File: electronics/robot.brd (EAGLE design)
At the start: 170.3 x 155.9 mm, 73 parts, among them IC1 FT232L, U1 MT3608, U2 ESP32-WROOM-32E_(16MB), U3 IRLMS2002TRPBF, U4 IRLMS2002TRPBF, X1 USB-B

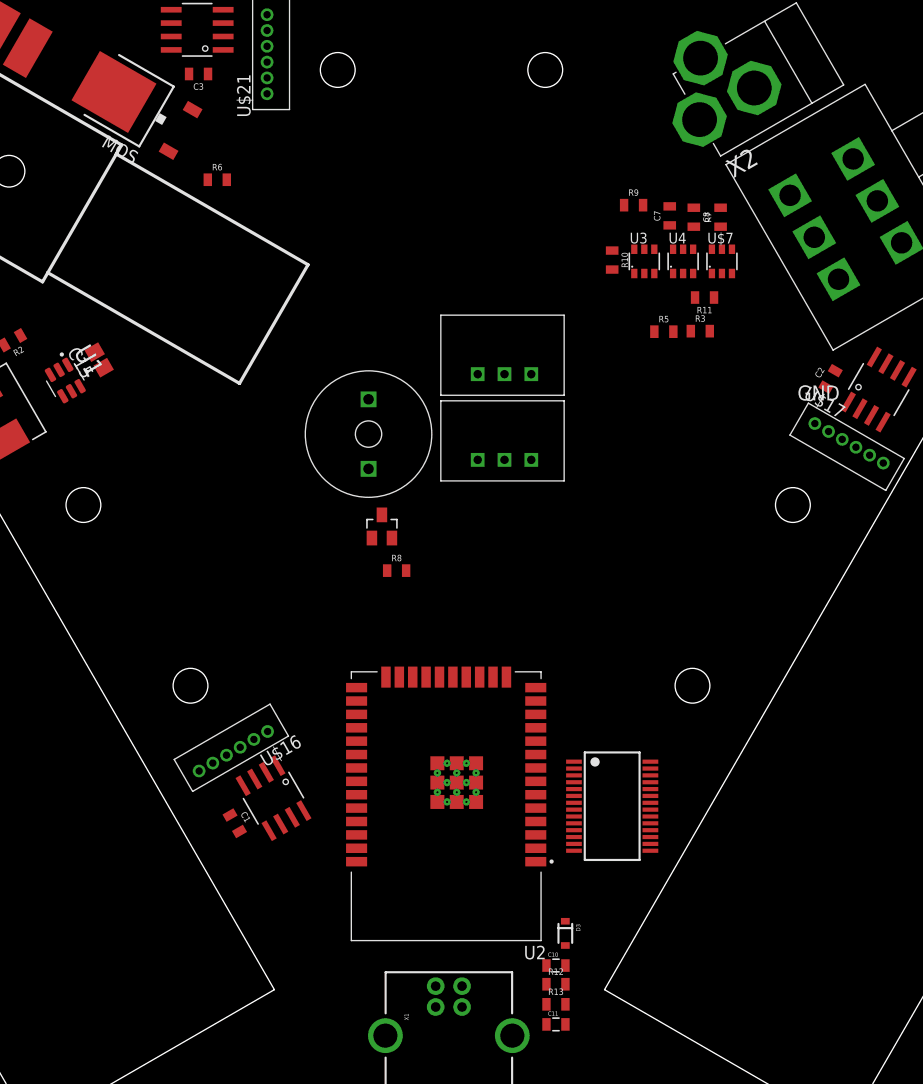
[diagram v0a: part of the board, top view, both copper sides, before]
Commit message: Removing former directories (electronics merged)
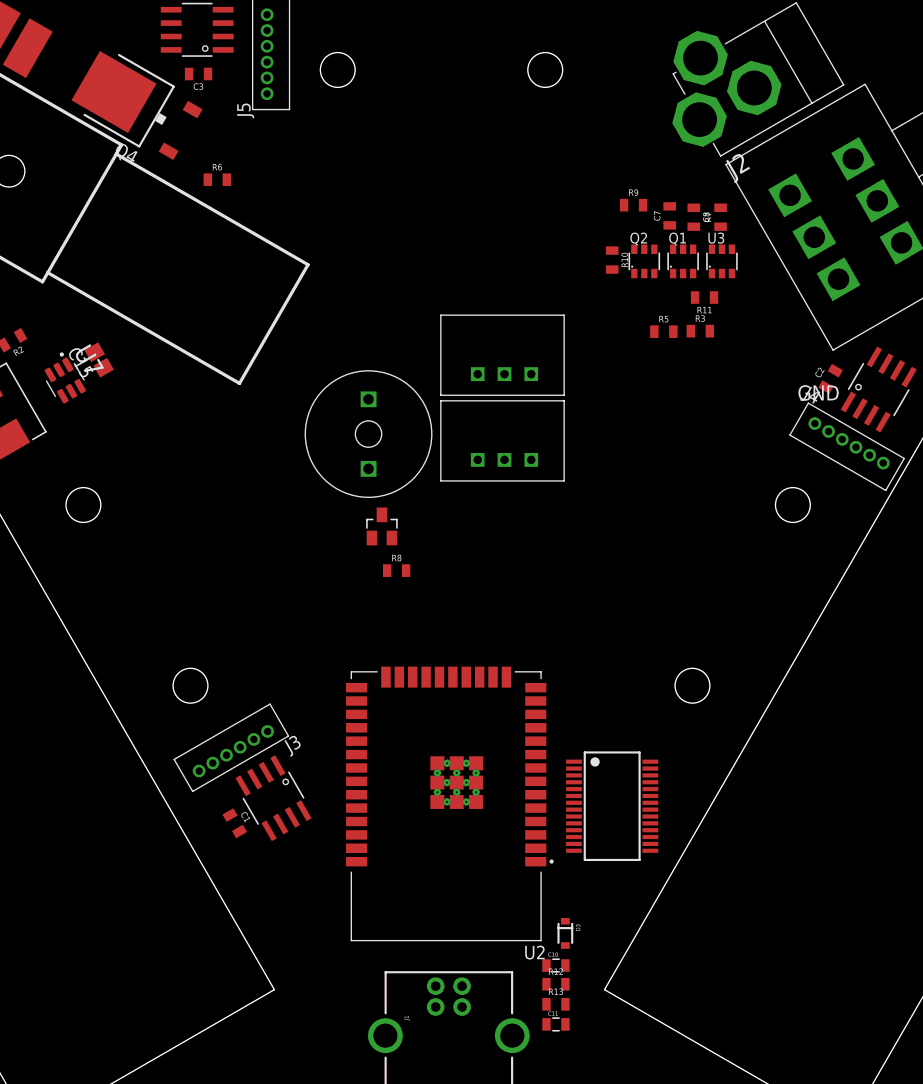
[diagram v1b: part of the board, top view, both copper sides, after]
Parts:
- removed HB1: L9110, rhoban:SO8
- removed IC1: FT232L, rhoban:SSOP28
- removed REG: REG_5V, rhoban:TRACOPOWER
- removed U$7: S8252, rhoban:SOT23-6
- added Q1, Q2: IRLMS2002TRPBF, rhoban:SOT23-6
- added REG2: REG_5V, rhoban:TRACOPOWER
- added U7: MT3608, MT3608:SOT95P280X145-6N
- U1: value MT3608 -> FT232L; device MT3608:SOT95P280X145-6N -> rhoban:SSOP28
- U3: value IRLMS2002TRPBF -> S8252
- U4: value IRLMS2002TRPBF -> L9110; device rhoban:SOT23-6 -> rhoban:SO8
- moved U1 65.7 mm to (16.5, -36.8), turned to 270 degrees
- moved U4 64.1 mm to (-15.6, -36.1), turned to 300 degrees
- moved REG1 8.13 mm to (0.25, 2.16)
- moved U3 7.37 mm to (26.9, 14.9)
- renumbered HB2 to U5, HB3 to U6, KICK_PADS to J6, MOS to Q4, U$12 to Q3, U$13 to B1, U$14 to S1, U$16 to J3, U$17 to J4, U$21 to J5, X1 to J1, X2 to J2
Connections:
- removed net VIN_RAW: C1.1, C2.1, C3.1, HB1.2, HB1.3, U5.2, U5.3, U6.2, U6.3
- net 3.3V: now also REG2.P$3, U1.20, U1.4; no longer IC1.20, IC1.4, REG1.P$3
- net GND: now also Q2.4, REG2.P$2, U1.18, U1.21, U1.25, U1.7, U4.5, U4.8, U7.2; no longer HB1.5, HB1.8, IC1.18, IC1.21, IC1.25, IC1.7, REG.P$2, U1.2, U3.4
- net GND_RAW: now also Q1.4, U3.6; no longer U$7.6, U4.4
- net M1A: now also U4.6; no longer HB1.6
- net M1B: now also U4.7; no longer HB1.7
- net M1P1: now also U4.1; no longer HB1.1
- net M1P2: now also U4.4; no longer HB1.4
- net N$1: now also U7.1; no longer U1.1
- net N$10: now also Q1.1, Q1.2, Q1.5, Q1.6, Q2.1, Q2.2, Q2.5, Q2.6; no longer U3.1, U3.2, U3.5, U3.6, U4.1, U4.2, U4.5, U4.6
- net N$11: now also Q2.3, U3.2; no longer U$7.2, U3.3
- net N$12: now also Q1.3, U3.1; no longer U$7.1, U4.3
- net N$13: now also U3.3; no longer U$7.3
- net N$14: now also U1.1; no longer IC1.1
- net N$15: now also U1.5; no longer IC1.5
- net N$4: now also U7.3; no longer U1.3
- net N$8: now also U3.5; no longer U$7.5
- net N$9: now also U3.4; no longer U$7.4
- net USBDM: now also U1.16; no longer IC1.16
- net USBDP: now also U1.15; no longer IC1.15
- net VCC: now also REG1.P$3; no longer REG.P$3
- net VIN: now also C1.1, C2.1, C3.1, REG2.P$1, U4.2, U4.3, U5.2, U5.3, U6.2, U6.3, U7.4, U7.5; no longer REG.P$1, U1.4, U1.5

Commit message: Autorouting to test
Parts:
- removed D3: (no value), SparkFun-DiscreteSemi:SOD-323
- removed R1: 270, SparkFun-Resistors:0805
- added C9: 0.1µF, SparkFun-Capacitors:0805
- added R14: 270, rcl:R2010
- R6: value 0.3OHM-0805-1/8W-1% -> 3K
- moved C16 5.98 mm to (-39.9, 10.7)
- moved R5 3.51 mm to (17.9, 8.38)
- moved R3 3.28 mm to (21.6, 8.38)
- moved C6 2.74 mm to (-0.76, 71.0)
- moved LED5 2.74 mm to (-0.64, 75.1)
- moved LED6 2.74 mm to (-0.64, 75.1)
- moved C3 2.43 mm to (-20.3, 32.9)
- moved LED1 2.36 mm to (66.7, -36.3)
- moved LED2 2.36 mm to (66.7, -36.3)
- moved C4 2.36 mm to (63.1, -34.1)
- moved R6 2.08 mm to (-22.6, 23.9), turned to 180 degrees
- moved R2 1.78 mm to (-38.6, 7.51)
- moved LED3 1.65 mm to (-66.3, -35.6)
- moved LED4 1.65 mm to (-66.3, -35.6)
- moved C5 1.65 mm to (-62.3, -33.9)
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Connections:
- removed net VUSB: D3.2, J1.VBUS
- new net N$6: U1.1, U2.34
- net GND: now also C9.2, R6.1; no longer R6.2
- net KICK: now also R6.2; no longer R6.1
- net N$14: now also U1.5; no longer U1.1
- net N$15: now also C9.1, U1.17; no longer U1.5, U2.34
- net N$2: now also R14.2; no longer R1.2
- net VCC: now also J1.VBUS, REG2.P$1; no longer D3.1
- net VIN: no longer REG2.P$1
- net VSTORE: now also R14.1; no longer R1.1
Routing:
- net GND: track 0.00 -> 608.9 mm, vias 0 -> 9
- net VCC: track 0.00 -> 393.5 mm, vias 0 -> 4
- net VIN: track 0.00 -> 250.4 mm, vias 0 -> 2
- net N$30: track 0.00 -> 173.1 mm, vias 0 -> 1
- net N$28: track 0.00 -> 170.8 mm, vias 0 -> 1
- net 3.3: track 0.00 -> 133.7 mm
- net LEDS: track 0.00 -> 102.2 mm, vias 0 -> 2
- net M3A: track 0.00 -> 94.2 mm, vias 0 -> 2
- net M3B: track 0.00 -> 92.4 mm, vias 0 -> 2
- net M3C2: track 0.00 -> 86.2 mm, vias 0 -> 1
- net M3C1: track 0.00 -> 78.1 mm, vias 0 -> 2
- net M2B: track 0.00 -> 77.0 mm, vias 0 -> 4
- net KICK: track 0.00 -> 75.0 mm, vias 0 -> 2
- net M2C2: track 0.00 -> 74.4 mm, vias 0 -> 3
- net M2A: track 0.00 -> 71.4 mm, vias 0 -> 4
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- added copper zone on layer 1, net GND
- added copper zone on layer 16, net GND

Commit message: BMS resistors
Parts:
- R10, R9: value 10K -> 470
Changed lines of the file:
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@@
 <attribute name="FARNELL" value="2447662" x="26.797" y="19.05" size="1.778" layer="27" rot="R90" display="off"/>
 </element>
-<element name="R9" library="SparkFun-Resistors" package="0805" value="10K" x="18.542" y="20.193">
+<element name="R9" library="SparkFun-Resistors" package="0805" value="470" x="18.542" y="20.193">
 <attribute name="PROD_ID" value="RES-11622" x="18.542" y="20.193" size="1.778" layer="27" display="off"/>
 <attribute name="VALUE" value="0.3" x="18.542" y="20.193" size="1.778" layer="27" display="off"/>
 <attribute name="FARNELL" value="2074334RL" x="18.542" y="20.193" size="1.778" layer="27" display="off"/>
 </element>
-<element name="R10" library="SparkFun-Resistors" package="0805" value="10K" x="16.51" y="14.986" rot="R270">
+<element name="R10" library="SparkFun-Resistors" package="0805" value="470" x="16.51" y="14.986" rot="R270">
 <attribute name="PROD_ID" value="RES-11622" x="16.51" y="14.986" size="1.778" layer="27" rot="R270" display="off"/>
 <attribute name="VALUE" value="0.3" x="16.51" y="14.986" size="1.778" layer="27" rot="R270" display="off"/>

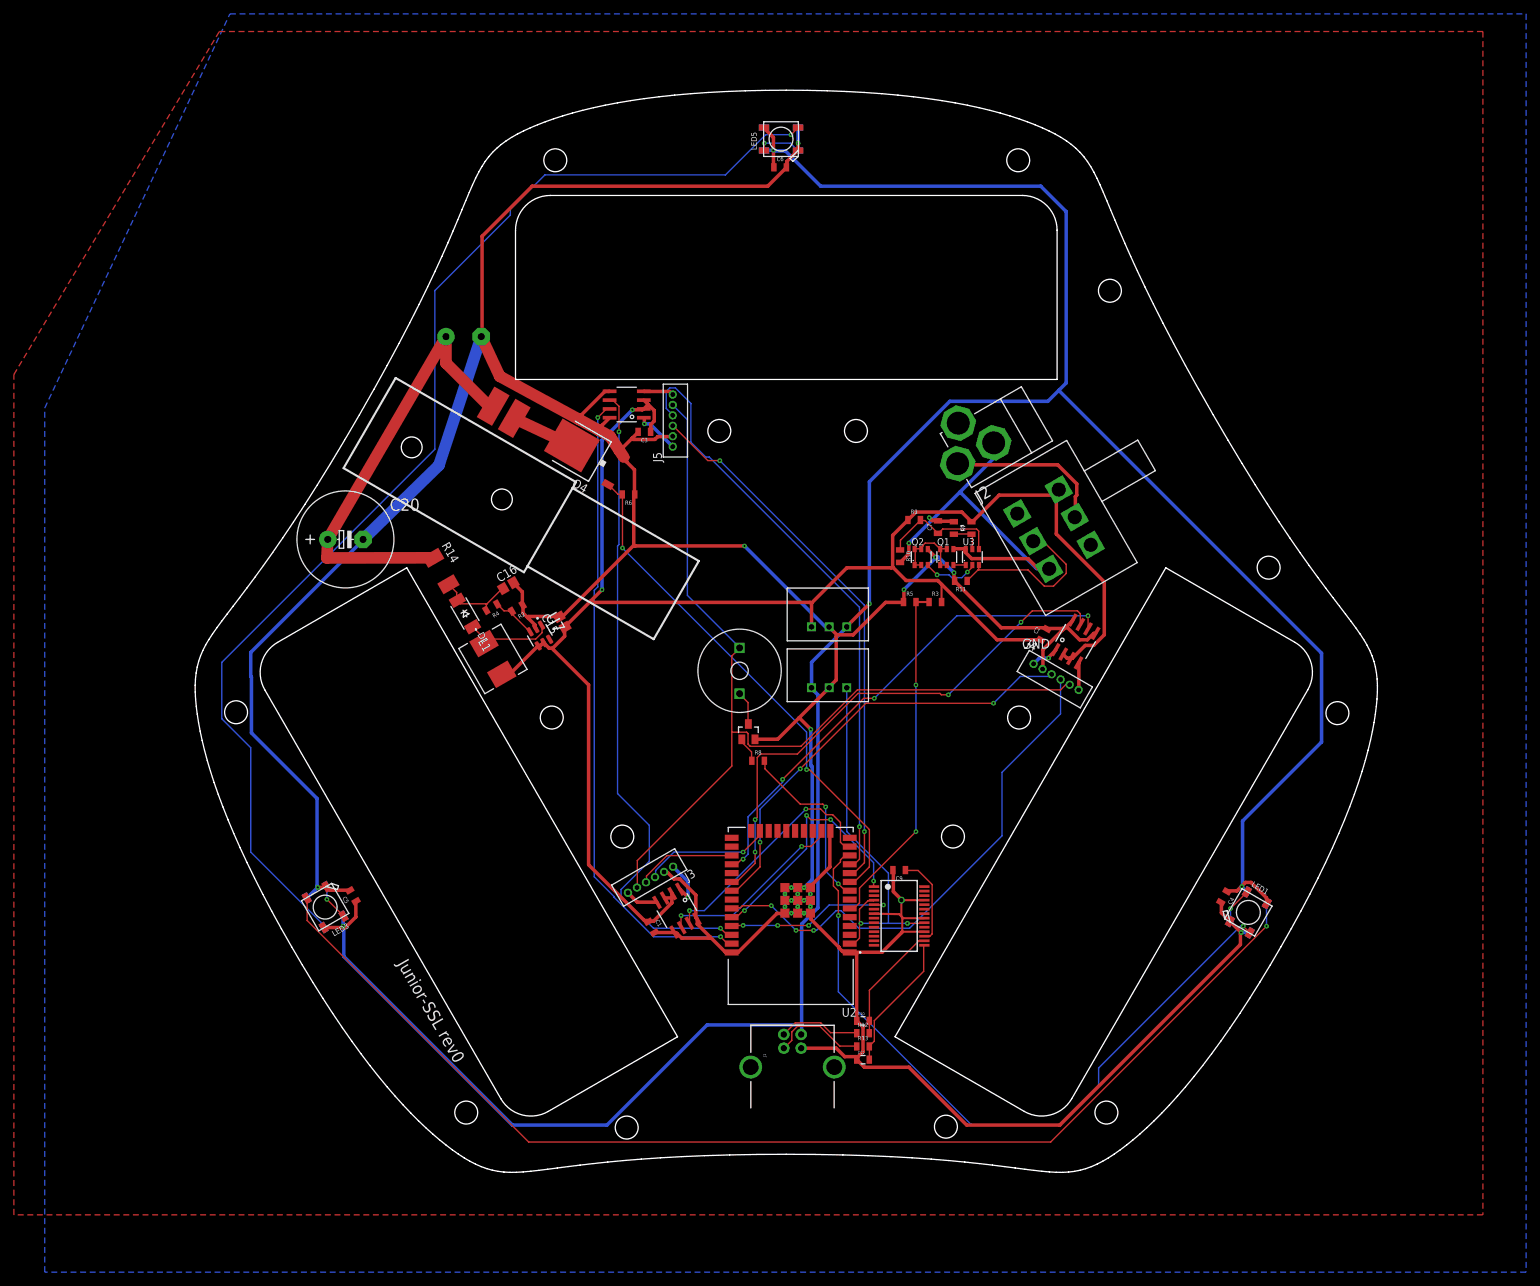
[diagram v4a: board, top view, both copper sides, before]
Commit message: DTR/RTS ESP programming and fixes
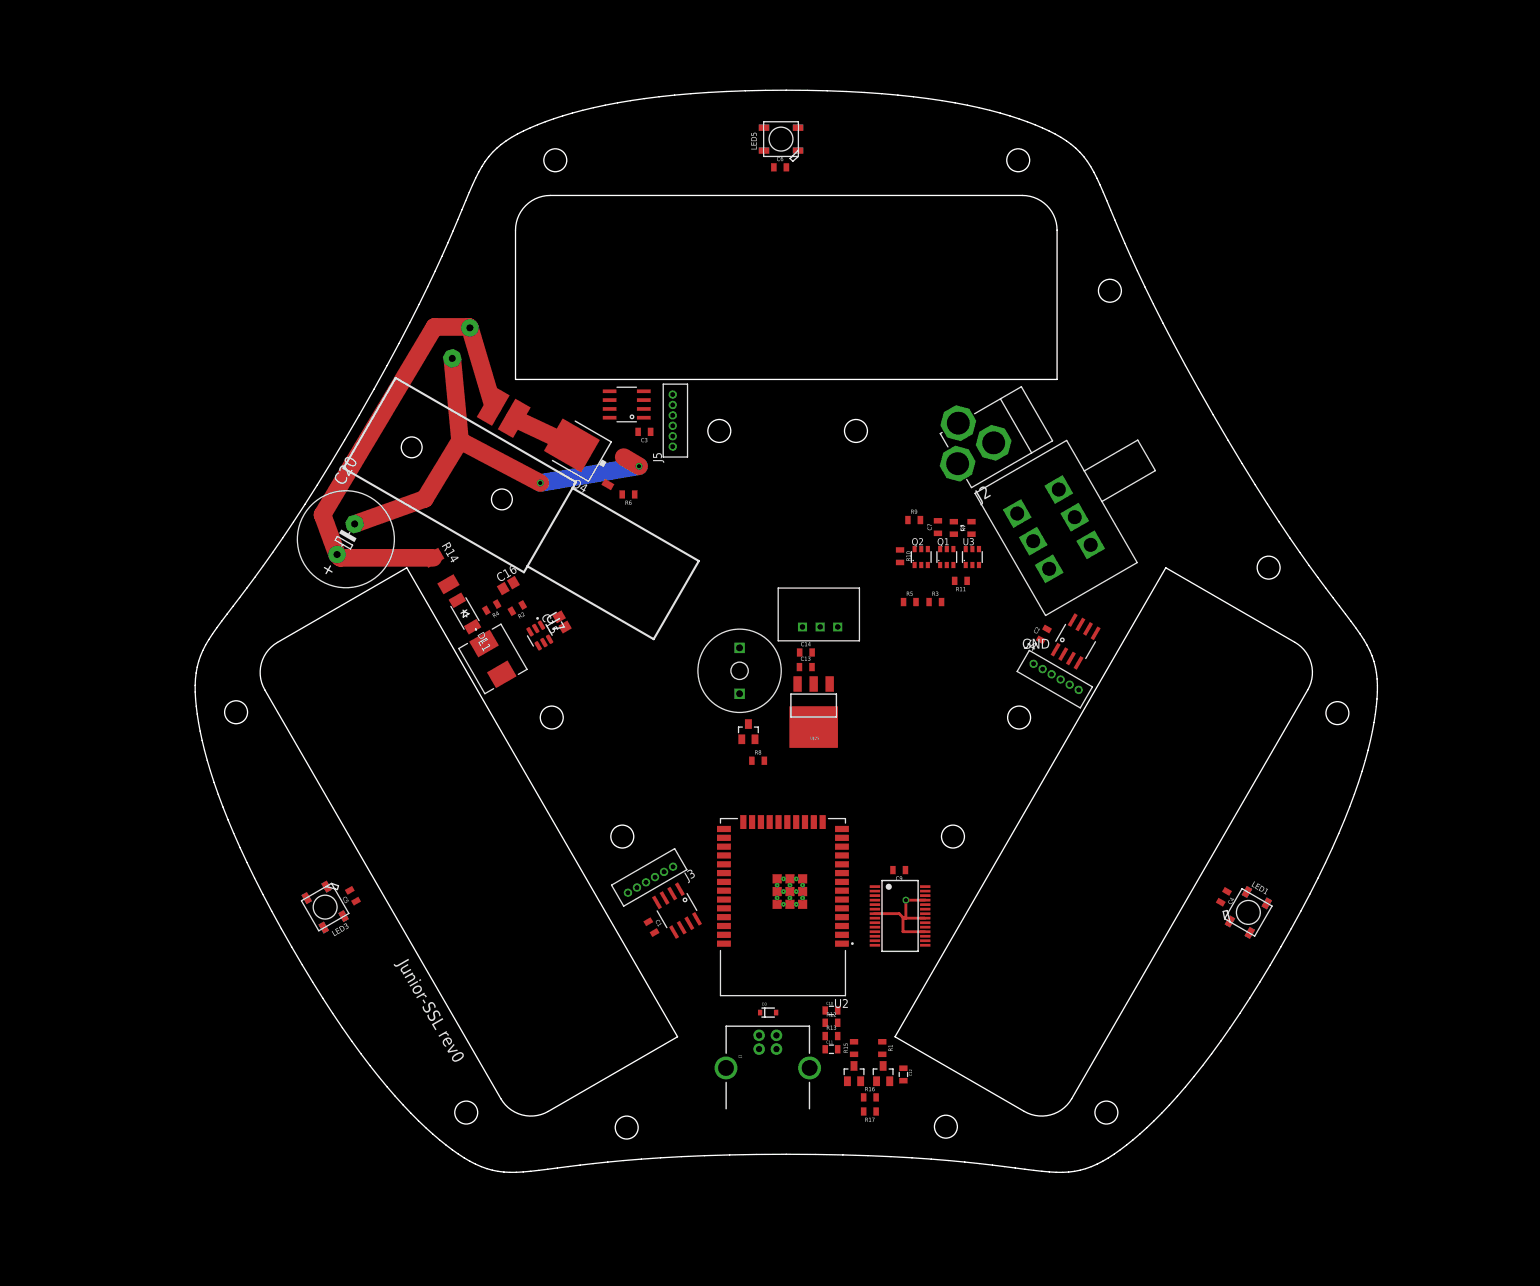
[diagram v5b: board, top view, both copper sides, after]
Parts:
- removed REG2: REG_5V, rhoban:TRACOPOWER
- added C12: 0.1uF, SparkFun-Passives:0805
- added C13: 1 µF, SparkFun-Capacitors:0805
- added C14: 0.1µF, SparkFun-Capacitors:0805
- added D3: (no value), SparkFun-DiscreteSemi:SOD-323
- added Q5, Q6: NPN_BC817,215, rhoban:SOT-23
- added R1, R16, R17: 10K, SparkFun-Resistors:0805
- added R15: 5K, SparkFun-Resistors:0805
- added U$25: TS2940CW-3.3RP, rhoban:SOT223
- moved C10 4.79 mm to (6.63, -50.4)
- moved C11 4.79 mm to (6.63, -56.0)
- moved R12 4.79 mm to (6.63, -52.2)
- moved R13 4.79 mm to (6.63, -54.1)
- moved J1 3.56 mm to (-2.54, -56.0)
- moved U2 1.69 mm to (-0.36, -35.6)
- moved REG1 1.30 mm to (-1.04, 2.79)
- moved C19 1.00 mm to (-46.7, 45.7), turned to 300 degrees
- moved U1 0.13 mm to (16.5, -36.8)
- moved C20 0.07 mm to (-63.3, 17.4), turned to 60 degrees
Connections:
- removed net 3.3: B1.P$2, J3.2, J4.2, J5.2
- new net DTR: Q6.2, R16.1, U1.2
- new net EN: C12.1, Q5.3, R1.2, U2.3
- new net IO0: Q6.3, R15.1, U2.25
- new net N$16: Q5.1, R16.2
- new net N$17: Q6.1, R17.2
- new net RTS: Q5.2, R17.1, U1.3
- new net VUSB: D3.2, J1.VBUS, U1.20
- net 3.3V: now also B1.P$2, C13.1, C14.1, J3.2, J4.2, J5.2, R1.1, R15.2, U$25.3; no longer REG2.P$3, U1.20, U1.4
- net GND: now also C12.2, C13.2, C14.2, U$25.2; no longer REG2.P$2
- net N$15: now also U1.4
- net VCC: now also D3.1, U$25.1; no longer J1.VBUS, REG2.P$1
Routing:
- net GND: track 608.9 -> 80.7 mm, vias 9 -> 3
- net VCC: track 393.5 -> 0.00 mm, vias 4 -> 0
- net VIN: track 250.4 -> 0.00 mm, vias 2 -> 0
- net N$30: track 173.1 -> 0.00 mm, vias 1 -> 0
- net N$28: track 170.8 -> 0.00 mm, vias 1 -> 0
- net 3.3: track 133.7 -> 0.00 mm
- net LEDS: track 102.2 -> 0.00 mm, vias 2 -> 0
- net M3A: track 94.2 -> 0.00 mm, vias 2 -> 0
- net M3B: track 92.4 -> 0.00 mm, vias 2 -> 0
- net M3C2: track 86.2 -> 0.00 mm, vias 1 -> 0
- net M3C1: track 78.1 -> 0.00 mm, vias 2 -> 0
- net M2B: track 77.0 -> 0.00 mm, vias 4 -> 0
- net KICK: track 75.0 -> 0.00 mm, vias 2 -> 0
- net M2C2: track 74.4 -> 0.00 mm, vias 3 -> 0
- net M2A: track 71.4 -> 0.00 mm, vias 4 -> 0
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- removed copper zone on layer 1, net GND
- removed copper zone on layer 16, net GND

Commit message: Minor fixes
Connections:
- removed net LEDS_SUITE: LED6.2-DOUT
- net GND: now also U1.26
- net M1C1: now also U2.26; no longer U2.23
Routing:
- net N$1: track 0.00 -> 2.93 mm
- net N$2: track 0.00 -> 2.64 mm
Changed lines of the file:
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@@
 <setting verticaltext="up"/>
 </settings>
-<grid distance="0.001" unitdist="inch" unit="inch" style="lines" multiple="2" display="yes" altdistance="0.25" altunitdist="mm" altunit="mm"/>
+<grid distance="0.0254" unitdist="mm" unit="mm" style="lines" multiple="2" display="yes" altdistance="0.25" altunitdist="mm" altunit="mm"/>
 <layers>
 <layer number="1" name="Top" color="4" fill="1" visible="yes" active="yes"/>
@@
 <contactref element="C13" pad="2"/>
 <contactref element="C14" pad="2"/>
+<contactref element="U1" pad="26"/>
 <wire x1="-66.09005625" y1="-32.6132375" x2="-68.94794375" y2="-34.2632375" width="0" layer="19" extent="1-16"/>
 <wire x1="-62.7435" y1="-33.1465875" x2="-66.09005625" y2="-32.6132375" width="0" layer="19" extent="1-1"/>
@@
 <wire x1="8.1444" y1="-40.82" x2="2.4794" y2="-35.155" width="0" layer="19" extent="1-1"/>
 <wire x1="12.885" y1="-36.505" x2="8.1444" y2="-40.82" width="0" layer="19" extent="1-1"/>
+<wire x1="20.135" y1="-33.905" x2="20.135" y2="-34.555" width="0" layer="19" extent="1-1"/>
 <wire x1="15.483" y1="-30.226" x2="17.3228" y2="-34.555" width="0" layer="19" extent="1-16"/>
 <wire x1="5.3594" y1="-23.31" x2="2.4794" y2="-31.485" width="0" layer="19" extent="1-1"/>
@@
 <wire x1="69.32894375" y1="-35.0252375" x2="-68.947940625" y2="-34.2632375" width="0" layer="19" extent="1-16"/>
 </signal>
-<signal name="LEDS_SUITE">
-<contactref element="LED6" pad="2-DOUT"/>
-</signal>
 <signal name="N$30">
 <contactref element="LED4" pad="2-DOUT"/>
@@
 <signal name="M1C1">
 <contactref element="J3" pad="4"/>
-<contactref element="U2" pad="23"/>
-<wire x1="-4.8006" y1="-23.31" x2="-18.7821125" y2="-31.239165625" width="0" layer="19" extent="1-1"/>
+<contactref element="U2" pad="26"/>
+<wire x1="-8.8556" y1="-25.58" x2="-18.7821125" y2="-31.239165625" width="0" layer="19" extent="1-1"/>
 </signal>
 <signal name="M1C2">
@@
 <contactref element="U7" pad="1"/>
 <contactref element="D1" pad="2"/>
-<wire x1="-45.05204375" y1="4.821184375" x2="-43.408521875" y2="2.40045625" width="0" layer="19" extent="1-1"/>
+<wire x1="-43.408521875" y1="2.40045625" x2="-45.05204375" y2="4.821184375" width="1.6764" layer="1"/>
 <wire x1="-35.136334375" y1="5.044246875" x2="-43.408521875" y2="2.40045625" width="0" layer="19" extent="1-1"/>
 </signal>
@@
 <contactref element="D1" pad="1"/>
 <contactref element="R14" pad="2"/>
-<wire x1="-48.527525" y1="10.938759375" x2="-47.252046875" y2="8.63169375" width="0" layer="19" extent="1-1"/>
+<wire x1="-47.252046875" y1="8.63169375" x2="-48.527525" y2="10.938759375" width="1.6764" layer="1"/>
 <wire x1="-43.082875" y1="7.18245" x2="-47.252046875" y2="8.63169375" width="0" layer="19" extent="1-1"/>
 <wire x1="-40.6435875" y1="10.318953125" x2="-43.082875" y2="7.18245" width="0" layer="19" extent="1-1"/>

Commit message: rev0
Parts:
- moved C19 0.47 mm to (-46.6, 45.2), flipped to the top, turned to 240 degrees
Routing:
- net VSTORE: track 68.6 -> 67.7 mm
